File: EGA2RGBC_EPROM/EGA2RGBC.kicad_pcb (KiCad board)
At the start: 2 copper layers, 59.7 x 45.1 mm, 21 parts, among them J1 EGA Input, J3 CSync Selection, J4 Power, J5 Video Out, U1 27C010, U2 74LS244

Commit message: Update schematics
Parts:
- added JP2: Brown Fix, Connector_PinHeader_2.54mm:PinHeader_1x02_P2.54mm_Vertical, F.Cu at (91.4, 57.8)
- added R9: 4.7k, Resistor_THT:R_Axial_DIN0204_L3.6mm_D1.6mm_P7.62mm_Horizontal, F.Cu at (105.4, 61.0)
- moved R8 7.75 mm to (97.8, 50.8), turned to 0 degrees
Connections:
- U1 pad 26: GND -> Net-(JP2-Pad2)
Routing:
- net VCC: track 94.4 -> 133.0 mm
- net Net-(JP2-Pad2): track 0.00 -> 29.0 mm
- net /DEC_B: track 37.6 -> 55.2 mm
- net GND: track 174.9 -> 179.3 mm
- net /MODE_IN: track 24.8 -> 26.7 mm
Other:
- board text added: "Brown Fix Disable"
- board text removed: "<-- Jumper for CGA"

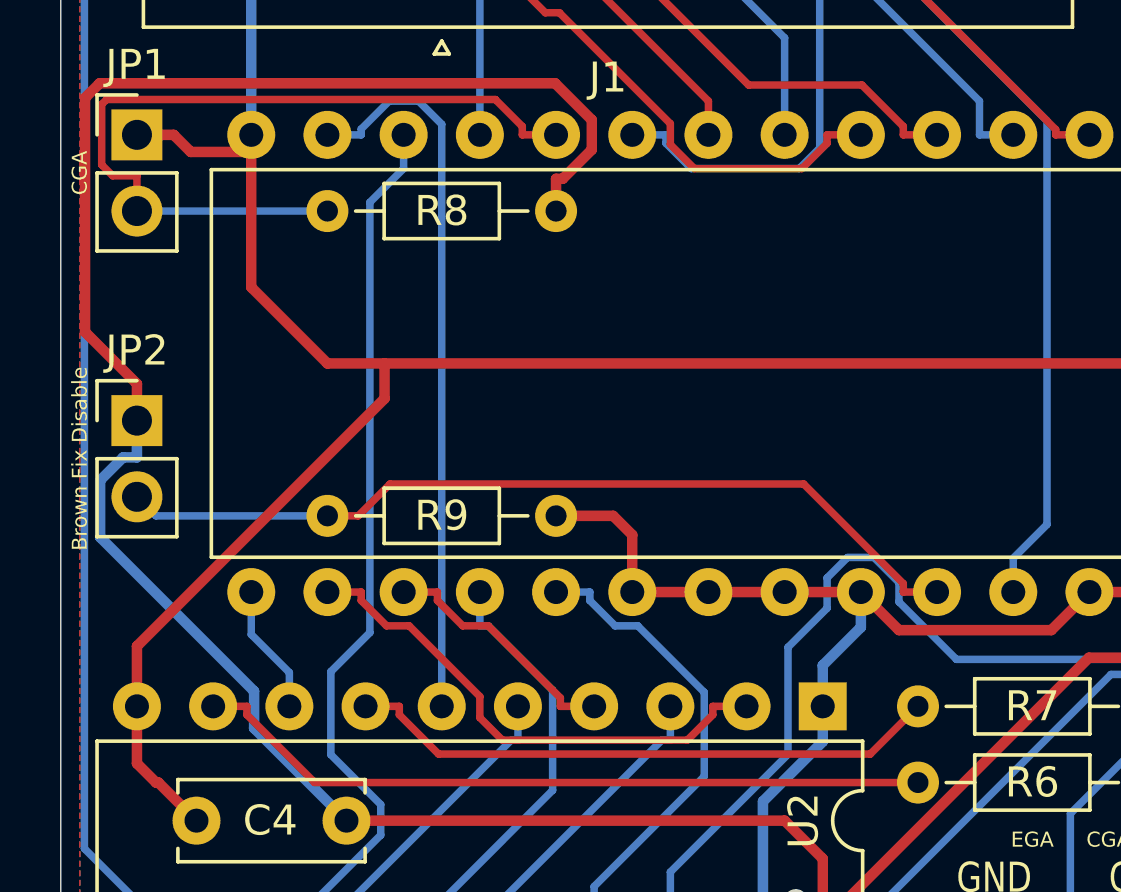
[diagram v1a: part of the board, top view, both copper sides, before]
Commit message: Moved resistors
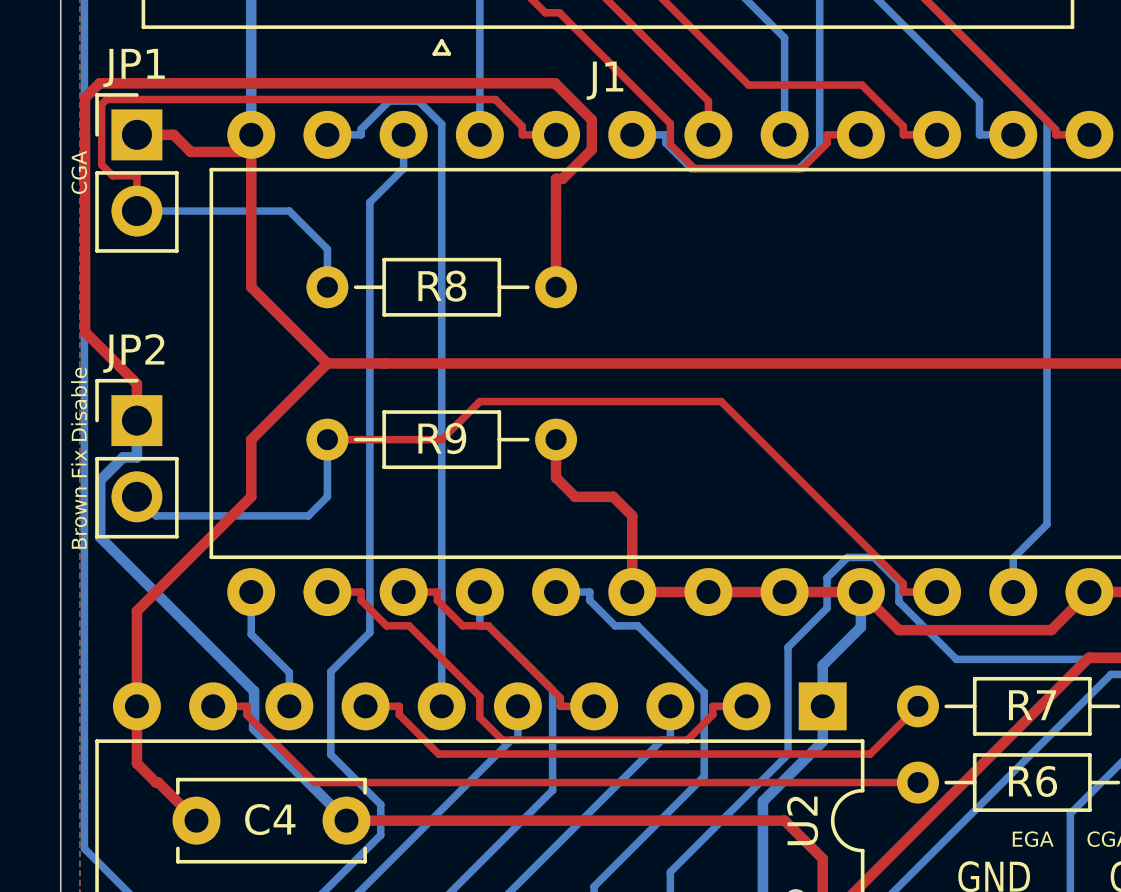
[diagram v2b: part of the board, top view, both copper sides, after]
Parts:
- moved R8 2.54 mm to (97.8, 53.3)
- moved R9 2.54 mm to (105.4, 58.4)
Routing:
- net Net-(JP2-Pad2): track 29.0 -> 32.4 mm
- net VCC: track 133.0 -> 135.6 mm
- net /MODE_IN: track 26.7 -> 28.5 mm
- net GND: track 179.3 -> 180.7 mm
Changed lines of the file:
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@@
     (thickness 1.6)
     (drawings 26)
-    (tracks 302)
+    (tracks 310)
     (zones 0)
     (modules 23)
@@
   (page A4)
   (layers
-    (0 F.Cu signal hide)
-    (31 B.Cu signal hide)
+    (0 F.Cu signal)
+    (31 B.Cu signal)
     (32 B.Adhes user)
     (33 F.Adhes user)
@@
   )
   (module Resistor_THT:R_Axial_DIN0204_L3.6mm_D1.6mm_P7.62mm_Horizontal (layer F.Cu)
-    (at 105.41 60.96 180)
+    (at 105.41 58.42 180)
     (descr "Resistor, Axial_DIN0204 series, Axial, Horizontal, pin pitch=7.62mm, 0.167W, length*diameter=3.6*1.6mm^2, http://cdn-reichelt.de/documents/datenblatt/B400/1_4W%23YAG.pdf")
     (tags "Resistor Axial_DIN0204 series Axial Horizontal pin pitch 7.62mm 0.167W length 3.6mm diameter 1.6mm")
@@
   )
   (module Resistor_THT:R_Axial_DIN0204_L3.6mm_D1.6mm_P7.62mm_Horizontal (layer F.Cu)
-    (at 97.79 50.8)
+    (at 97.79 53.34)
     (descr "Resistor, Axial_DIN0204 series, Axial, Horizontal, pin pitch=7.62mm, 0.167W, length*diameter=3.6*1.6mm^2, http://cdn-reichelt.de/documents/datenblatt/B400/1_4W%23YAG.pdf")
     (tags "Resistor Axial_DIN0204 series Axial Horizontal pin pitch 7.62mm 0.167W length 3.6mm diameter 1.6mm")
@@
   (segment (start 100.425 41.91) (end 100.115 42.22) (width 0.35) (layer B.Cu) (net 1))
   (segment (start 100.115 42.22) (end 95.25 42.22) (width 0.35) (layer B.Cu) (net 1))
-  (segment (start 105.41 60.96) (end 107.315 60.96) (width 0.35) (layer F.Cu) (net 1))
-  (segment (start 107.315 60.96) (end 107.95 61.595) (width 0.35) (layer F.Cu) (net 1))
-  (segment (start 107.95 61.595) (end 107.95 63.5) (width 0.35) (layer F.Cu) (net 1))
   (segment (start 125.81 55.88) (end 125.81 63.42) (width 0.35) (layer F.Cu) (net 1))
   (segment (start 125.81 63.42) (end 125.73 63.5) (width 0.35) (layer F.Cu) (net 1))
@@
   (segment (start 135.622 52.705) (end 139.065 52.705) (width 0.35) (layer B.Cu) (net 1))
   (segment (start 125.81 55.88) (end 99.6935 55.88) (width 0.35) (layer F.Cu) (net 1))
-  (segment (start 99.6935 55.88) (end 99.6935 57.0515) (width 0.35) (layer F.Cu) (net 1))
-  (segment (start 99.6935 57.0515) (end 91.44 65.305) (width 0.35) (layer F.Cu) (net 1))
-  (segment (start 91.44 65.305) (end 91.44 67.31) (width 0.35) (layer F.Cu) (net 1))
   (segment (start 128.27 48.26) (end 127.095 48.26) (width 0.35) (layer B.Cu) (net 1))
   (segment (start 127.095 48.26) (end 126.412 47.5776) (width 0.35) (layer B.Cu) (net 1))
@@
   (segment (start 121.92 64.77) (end 123.19 63.5) (width 0.35) (layer F.Cu) (net 1))
   (segment (start 116.84 64.77) (end 121.92 64.77) (width 0.35) (layer F.Cu) (net 1))
+  (segment (start 105.41 59.69) (end 105.41 58.42) (width 0.35) (layer F.Cu) (net 1))
+  (segment (start 106.045 60.325) (end 105.41 59.69) (width 0.35) (layer F.Cu) (net 1))
+  (segment (start 107.315 60.325) (end 106.045 60.325) (width 0.35) (layer F.Cu) (net 1))
+  (segment (start 107.95 60.96) (end 107.315 60.325) (width 0.35) (layer F.Cu) (net 1))
+  (segment (start 107.95 63.5) (end 107.95 60.96) (width 0.35) (layer F.Cu) (net 1))
+  (segment (start 95.25 58.42) (end 97.79 55.88) (width 0.35) (layer F.Cu) (net 1))
+  (segment (start 95.25 60.325) (end 95.25 58.42) (width 0.35) (layer F.Cu) (net 1))
+  (segment (start 91.44 64.135) (end 95.25 60.325) (width 0.35) (layer F.Cu) (net 1))
+  (segment (start 91.44 67.31) (end 91.44 64.135) (width 0.35) (layer F.Cu) (net 1))
   (segment (start 105.41 50.8) (end 105.41 49.7247) (width 0.35) (layer F.Cu) (net 2))
   (segment (start 91.44 57.785) (end 91.44 56.5597) (width 0.35) (layer F.Cu) (net 2))
@@
   (segment (start 129.635 63.8653) (end 129.635 63.5) (width 0.35) (layer F.Cu) (net 2))
   (segment (start 129.635 63.5) (end 130.81 63.5) (width 0.35) (layer F.Cu) (net 2))
+  (segment (start 105.41 50.8) (end 105.41 53.34) (width 0.35) (layer F.Cu) (net 2))
   (segment (start 146.685 56.515) (end 146.685 62.1) (width 0.35) (layer F.Cu) (net 3))
   (segment (start 146.685 62.1) (end 146.815 62.23) (width 0.35) (layer F.Cu) (net 3))
@@
   (segment (start 101.0244 39.2563) (end 102.87 41.1019) (width 0.25) (layer B.Cu) (net 33))
   (segment (start 102.87 41.1019) (end 102.87 48.26) (width 0.25) (layer B.Cu) (net 33))
-  (segment (start 97.79 50.8) (end 91.44 50.8) (width 0.25) (layer B.Cu) (net 34))
   (segment (start 105.41 48.26) (end 104.285 48.26) (width 0.25) (layer F.Cu) (net 34))
   (segment (start 104.285 48.26) (end 104.285 47.9787) (width 0.25) (layer F.Cu) (net 34))
@@
   (segment (start 90.6319 49.6247) (end 91.44 49.6247) (width 0.25) (layer F.Cu) (net 34))
   (segment (start 91.44 49.6247) (end 91.44 50.8) (width 0.25) (layer F.Cu) (net 34))
-  (segment (start 118.11 63.5) (end 116.9847 63.5) (width 0.25) (layer F.Cu) (net 35))
-  (segment (start 97.79 60.96) (end 98.8153 60.96) (width 0.25) (layer F.Cu) (net 35))
-  (segment (start 98.8153 60.96) (end 99.8764 59.8989) (width 0.25) (layer F.Cu) (net 35))
-  (segment (start 99.8764 59.8989) (end 113.6649 59.8989) (width 0.25) (layer F.Cu) (net 35))
-  (segment (start 113.6649 59.8989) (end 116.9847 63.2187) (width 0.25) (layer F.Cu) (net 35))
+  (segment (start 91.44 50.8) (end 96.52 50.8) (width 0.25) (layer B.Cu) (net 34))
+  (segment (start 97.79 52.07) (end 97.79 53.34) (width 0.25) (layer B.Cu) (net 34))
+  (segment (start 96.52 50.8) (end 97.79 52.07) (width 0.25) (layer B.Cu) (net 34))
+  (segment (start 97.79 60.325) (end 97.79 58.42) (width 0.25) (layer B.Cu) (net 35))
+  (segment (start 97.155 60.96) (end 97.79 60.325) (width 0.25) (layer B.Cu) (net 35))
+  (segment (start 92.075 60.96) (end 97.155 60.96) (width 0.25) (layer B.Cu) (net 35))
+  (segment (start 91.44 60.325) (end 92.075 60.96) (width 0.25) (layer B.Cu) (net 35))
+  (segment (start 116.9847 63.5) (end 118.11 63.5) (width 0.25) (layer F.Cu) (net 35))
   (segment (start 116.9847 63.2187) (end 116.9847 63.5) (width 0.25) (layer F.Cu) (net 35))
-  (segment (start 97.79 60.96) (end 92.075 60.96) (width 0.25) (layer B.Cu) (net 35))
-  (segment (start 92.075 60.96) (end 91.44 60.325) (width 0.25) (layer B.Cu) (net 35))
+  (segment (start 102.87 57.15) (end 110.916 57.15) (width 0.25) (layer F.Cu) (net 35))
+  (segment (start 110.916 57.15) (end 116.9847 63.2187) (width 0.25) (layer F.Cu) (net 35))
+  (segment (start 101.6 58.42) (end 102.87 57.15) (width 0.25) (layer F.Cu) (net 35))
+  (segment (start 97.79 58.42) (end 101.6 58.42) (width 0.25) (layer F.Cu) (net 35))
   (zone (net 1) (net_name GND) (layer B.Cu) (hatch edge 0.508)
     (connect_pads (clearance 0.508))

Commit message: Create rev 1.1
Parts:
- C4, C5: footprint Capacitor_THT:C_Disc_D6.0mm_W2.5mm_P5.00mm -> Capacitor_THT:C_Disc_D3.0mm_W2.0mm_P2.50mm
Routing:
- net GND: track 180.7 -> 185.7 mm
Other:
- board text added: "rev 1.1"
- board text removed: "CGA"
- board text removed: "rev 1.0"
